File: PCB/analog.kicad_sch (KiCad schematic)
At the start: 26 parts, among them U3 74HC4051, U4 OPA350, U5 74HC4051

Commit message: Update and pre-production output
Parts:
- C10, C12, C13: LCSC (none) -> C307331
- C11: footprint Capacitor_SMD:C_0402_1005Metric -> Capacitor_SMD:C_0603_1608Metric; LCSC (none) -> C302060
- JP1: footprint Resistor_SMD:R_0603_1608Metric_Pad0.98x0.95mm_HandSolder -> Resistor_SMD:R_0603_1608Metric
- R13, R14, R15, R16, R17, R18, R19, R20, R23, R24, R25, R26, R27, R28, R29, R30: LCSC (none) -> C25741
- R21: footprint Resistor_SMD:R_0402_1005Metric -> Resistor_SMD:R_0603_1608Metric; LCSC (none) -> C25803
- R22: footprint Resistor_SMD:R_0402_1005Metric -> Resistor_SMD:R_0603_1608Metric; LCSC (none) -> C21190
- U3, U5: LCSC (none) -> C5645
- U4: LCSC (none) -> C13388
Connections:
- net COL0: now also R16.1, U3.12 (A3); no longer R13.1, U3.13 (A0)
- net COL1: now also R13.1, U3.13 (A0); no longer R16.1, U3.12 (A3)
- net COL12: now also R27.1, U5.1 (A4); no longer R28.1, U5.5 (A5)
- net COL13: now also R29.1, U5.2 (A6); no longer R30.1, U5.4 (A7)
- net COL14: now also R30.1, U5.4 (A7); no longer R27.1, R29.1, U5.1 (A4), U5.2 (A6)
- net COL4: now also R17.1, U3.1 (A4); no longer R18.1, U3.5 (A5)
- net COL5: now also R19.1, U3.2 (A6); no longer R20.1, U3.4 (A7)
- net COL6: now also R20.1, U3.4 (A7); no longer R19.1, U3.2 (A6)
- net COL7: now also R18.1, U3.5 (A5); no longer R17.1, U3.1 (A4)
- net COL8: now also R26.1, U5.12 (A3); no longer R23.1, U5.13 (A0)
- net COL9: now also R23.1, U5.13 (A0); no longer R26.1, U5.12 (A3)
- new net COL15: R28.1, U5.5 (A5)

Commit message: Schematic update
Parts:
- C11: LCSC C302060 -> C1603
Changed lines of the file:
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@@
       (effects (font (size 1.27 1.27)) hide)
     )
-    (property "LCSC" "C302060" (id 4) (at 202.565 90.17 0)
+    (property "LCSC" "C1603" (id 4) (at 202.565 90.17 0)
       (effects (font (size 1.27 1.27)) hide)
     )

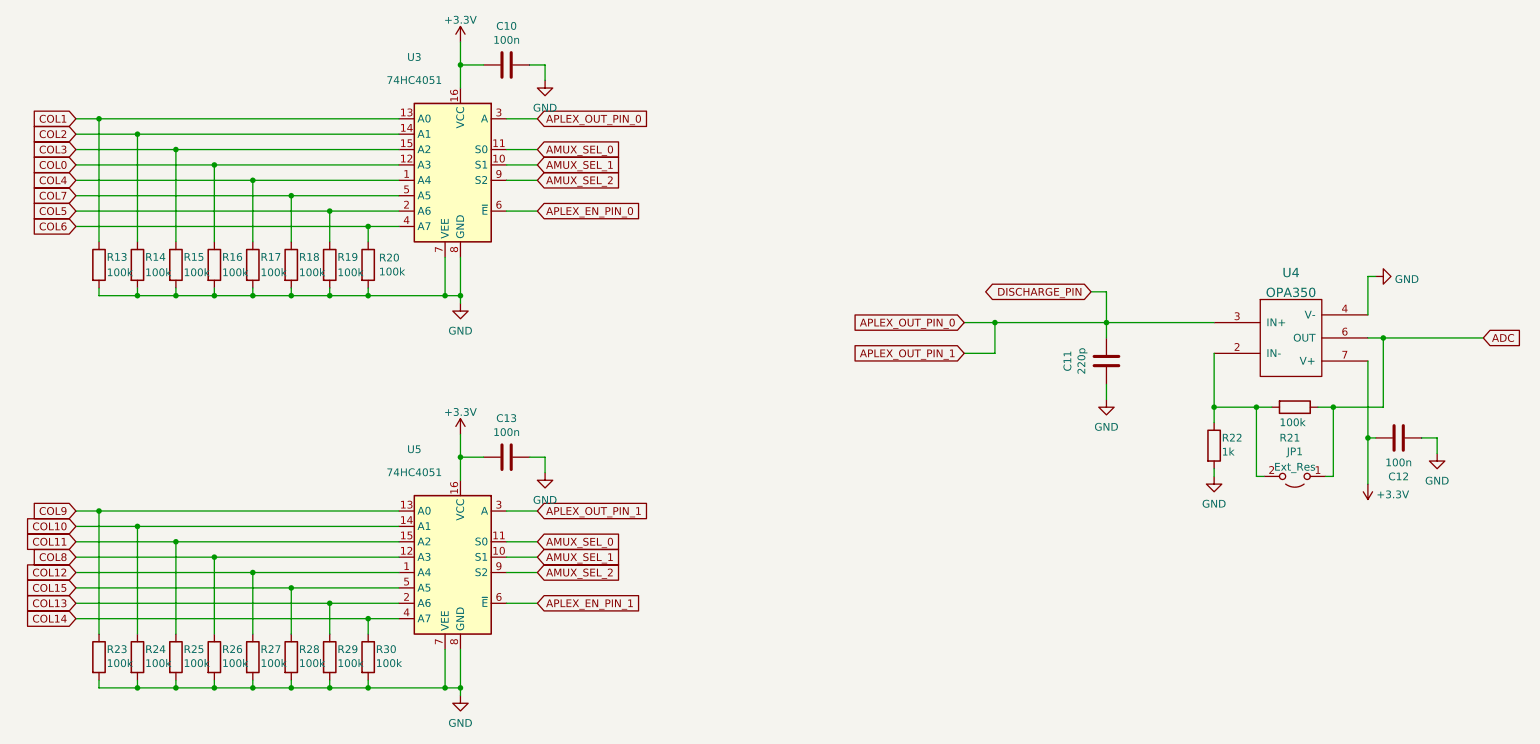
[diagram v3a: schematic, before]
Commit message: Update of PCB
Added shielding copper pad for plate electrical connection, along with EMI filtering through capacitor and inductor.
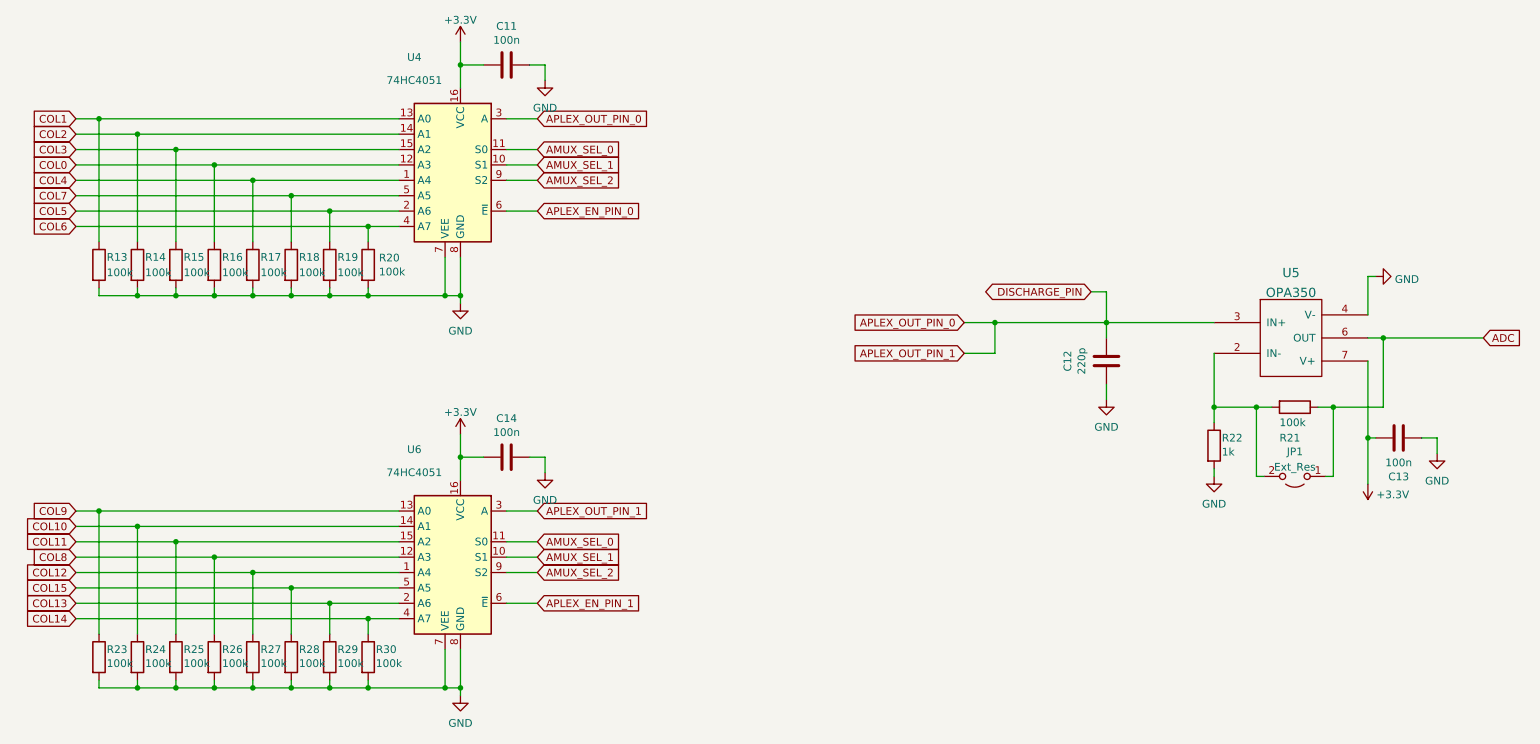
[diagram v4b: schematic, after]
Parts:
- renumbered C10 to C11, C11 to C12, C12 to C13, C13 to C14, U3 to U4, U4 to U5, U5 to U6
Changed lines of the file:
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@@
   (symbol (lib_id "74xx:74HC4051") (at 95.885 57.785 0) (mirror y) (unit 1)
     (in_bom yes) (on_board yes)
-    (property "Reference" "U3" (id 0) (at 88.265 40.005 0))
+    (property "Reference" "U4" (id 0) (at 88.265 40.005 0))
     (property "Value" "74HC4051" (id 1) (at 88.265 43.815 0))
     (property "Footprint" "cipulot_parts:TSSOP16" (id 2) (at 95.885 67.945 0)
@@
   (symbol (lib_id "power:GND") (at 202.565 96.52 0) (unit 1)
     (in_bom yes) (on_board yes) (fields_autoplaced)
-    (property "Reference" "#PWR051" (id 0) (at 202.565 102.87 0)
+    (property "Reference" "#PWR060" (id 0) (at 202.565 102.87 0)
       (effects (font (size 1.27 1.27)) hide)
     )
@@
   (symbol (lib_id "power:GND") (at 109.855 43.815 0) (unit 1)
     (in_bom yes) (on_board yes) (fields_autoplaced)
-    (property "Reference" "#PWR048" (id 0) (at 109.855 50.165 0)
+    (property "Reference" "#PWR057" (id 0) (at 109.855 50.165 0)
       (effects (font (size 1.27 1.27)) hide)
     )
@@
   (symbol (lib_id "power:GND") (at 220.345 109.22 0) (unit 1)
     (in_bom yes) (on_board yes) (fields_autoplaced)
-    (property "Reference" "#PWR055" (id 0) (at 220.345 115.57 0)
+    (property "Reference" "#PWR064" (id 0) (at 220.345 115.57 0)
       (effects (font (size 1.27 1.27)) hide)
     )
@@
   (symbol (lib_id "74xx:74HC4051") (at 95.885 122.555 0) (mirror y) (unit 1)
     (in_bom yes) (on_board yes)
-    (property "Reference" "U5" (id 0) (at 88.265 104.775 0))
+    (property "Reference" "U6" (id 0) (at 88.265 104.775 0))
     (property "Value" "74HC4051" (id 1) (at 88.265 108.585 0))
     (property "Footprint" "cipulot_parts:TSSOP16" (id 2) (at 95.885 132.715 0)
@@
   (symbol (lib_id "Device:C") (at 202.565 90.17 0) (unit 1)
     (in_bom yes) (on_board yes)
-    (property "Reference" "C11" (id 0) (at 196.1642 90.17 90))
+    (property "Reference" "C12" (id 0) (at 196.1642 90.17 90))
     (property "Value" "220p" (id 1) (at 198.4756 90.17 90))
     (property "Footprint" "Capacitor_SMD:C_0603_1608Metric" (id 2) (at 203.5302 93.98 0)
@@
   (symbol (lib_id "power:GND") (at 247.015 76.2 90) (unit 1)
     (in_bom yes) (on_board yes) (fields_autoplaced)
-    (property "Reference" "#PWR049" (id 0) (at 253.365 76.2 0)
+    (property "Reference" "#PWR058" (id 0) (at 253.365 76.2 0)
       (effects (font (size 1.27 1.27)) hide)
     )
@@
   (symbol (lib_id "power:GND") (at 109.855 108.585 0) (unit 1)
     (in_bom yes) (on_board yes) (fields_autoplaced)
-    (property "Reference" "#PWR054" (id 0) (at 109.855 114.935 0)
+    (property "Reference" "#PWR063" (id 0) (at 109.855 114.935 0)
       (effects (font (size 1.27 1.27)) hide)
     )
@@
   (symbol (lib_id "power:GND") (at 257.175 105.41 0) (unit 1)
     (in_bom yes) (on_board yes) (fields_autoplaced)
-    (property "Reference" "#PWR053" (id 0) (at 257.175 111.76 0)
+    (property "Reference" "#PWR062" (id 0) (at 257.175 111.76 0)
       (effects (font (size 1.27 1.27)) hide)
     )
@@
   (symbol (lib_id "Device:C") (at 103.505 106.045 270) (unit 1)
     (in_bom yes) (on_board yes)
-    (property "Reference" "C13" (id 0) (at 103.505 99.6442 90))
+    (property "Reference" "C14" (id 0) (at 103.505 99.6442 90))
     (property "Value" "100n" (id 1) (at 103.505 101.9556 90))
     (property "Footprint" "Capacitor_SMD:C_0402_1005Metric" (id 2) (at 99.695 107.0102 0)
@@
   (symbol (lib_id "power:GND") (at 95.885 80.645 0) (unit 1)
     (in_bom yes) (on_board yes) (fields_autoplaced)
-    (property "Reference" "#PWR050" (id 0) (at 95.885 86.995 0)
+    (property "Reference" "#PWR059" (id 0) (at 95.885 86.995 0)
       (effects (font (size 1.27 1.27)) hide)
     )
@@
   (symbol (lib_id "power:+3.3V") (at 95.885 37.465 0) (unit 1)
     (in_bom yes) (on_board yes) (fields_autoplaced)
-    (property "Reference" "#PWR047" (id 0) (at 95.885 41.275 0)
+    (property "Reference" "#PWR056" (id 0) (at 95.885 41.275 0)
       (effects (font (size 1.27 1.27)) hide)
     )
@@
   (symbol (lib_id "Device:C") (at 250.825 102.87 270) (mirror x) (unit 1)
     (in_bom yes) (on_board yes)
-    (property "Reference" "C12" (id 0) (at 250.825 109.2708 90))
+    (property "Reference" "C13" (id 0) (at 250.825 109.2708 90))
     (property "Value" "100n" (id 1) (at 250.825 106.9594 90))
     (property "Footprint" "Capacitor_SMD:C_0402_1005Metric" (id 2) (at 247.015 101.9048 0)
@@
   (symbol (lib_id "burrbrown:OPA350") (at 227.965 86.36 0) (mirror x) (unit 1)
     (in_bom yes) (on_board yes)
-    (property "Reference" "U4" (id 0) (at 233.045 75.6061 0)
+    (property "Reference" "U5" (id 0) (at 233.045 75.6061 0)
       (effects (font (size 1.524 1.524)))
     )
@@
   (symbol (lib_id "power:GND") (at 95.885 145.415 0) (unit 1)
     (in_bom yes) (on_board yes) (fields_autoplaced)
-    (property "Reference" "#PWR057" (id 0) (at 95.885 151.765 0)
+    (property "Reference" "#PWR066" (id 0) (at 95.885 151.765 0)
       (effects (font (size 1.27 1.27)) hide)
     )
@@
   (symbol (lib_id "Device:C") (at 103.505 41.275 270) (unit 1)
     (in_bom yes) (on_board yes)
-    (property "Reference" "C10" (id 0) (at 103.505 34.8742 90))
+    (property "Reference" "C11" (id 0) (at 103.505 34.8742 90))
     (property "Value" "100n" (id 1) (at 103.505 37.1856 90))
     (property "Footprint" "Capacitor_SMD:C_0402_1005Metric" (id 2) (at 99.695 42.2402 0)
@@
   (symbol (lib_id "power:+3.3V") (at 245.745 110.49 180) (unit 1)
     (in_bom yes) (on_board yes) (fields_autoplaced)
-    (property "Reference" "#PWR056" (id 0) (at 245.745 106.68 0)
+    (property "Reference" "#PWR065" (id 0) (at 245.745 106.68 0)
       (effects (font (size 1.27 1.27)) hide)
     )
@@
   (symbol (lib_id "power:+3.3V") (at 95.885 102.235 0) (unit 1)
     (in_bom yes) (on_board yes) (fields_autoplaced)
-    (property "Reference" "#PWR052" (id 0) (at 95.885 106.045 0)
-      (effects (font (size 1.27 1.27)) hide)
-    )
+    (property "Reference" "#PWR061" (id 0) (at 95.885 106.045 0)
+      (effects (font (size 1.27 1.27)) hide)
+    )
